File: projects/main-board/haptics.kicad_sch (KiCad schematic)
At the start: 10 parts, among them Q1 ZXTN4240F-7, Q2 ZXTN4240F-7, U12 TLV74330PDBVR

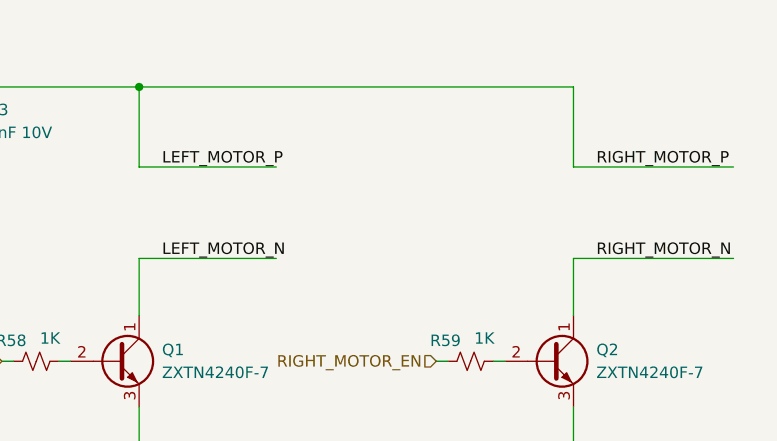
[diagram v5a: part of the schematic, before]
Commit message: Fix footprint DRC errors.
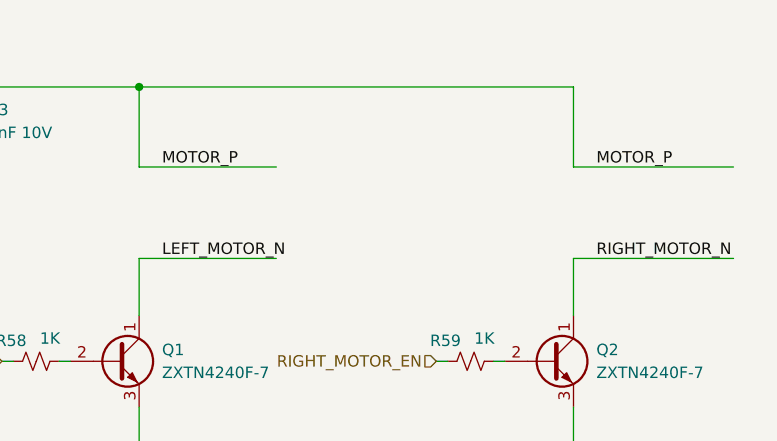
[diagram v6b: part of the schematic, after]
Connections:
- net LEFT_MOTOR_P renamed MOTOR_P
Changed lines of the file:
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@@
 		)
 	)
-	(label "LEFT_MOTOR_P"
+	(label "MOTOR_P"
 		(at 168.91 86.36 0)
 		(effects
@@
 		)
 	)
-	(label "RIGHT_MOTOR_P"
+	(label "MOTOR_P"
 		(at 217.17 86.36 0)
 		(effects

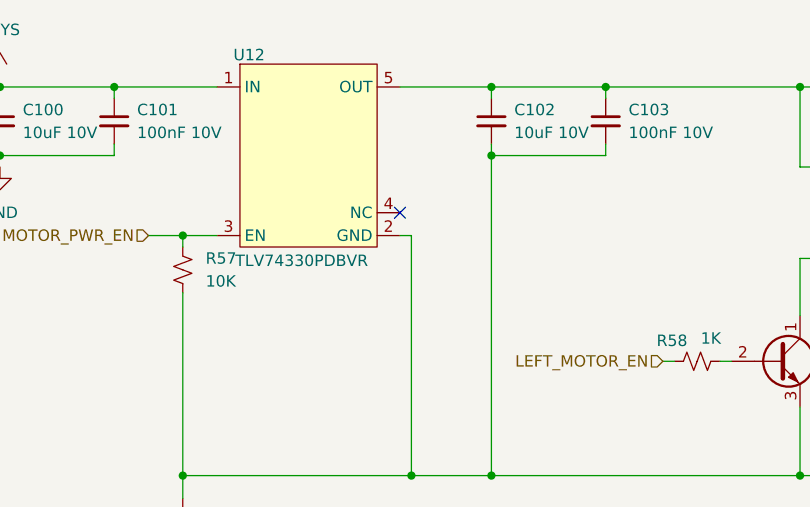
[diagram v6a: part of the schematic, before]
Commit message: Main board PCB layout and routing
- Add 48MHz crystal for STM32
- Add 32kHz crystal for STM32
- Started laying out and routing board
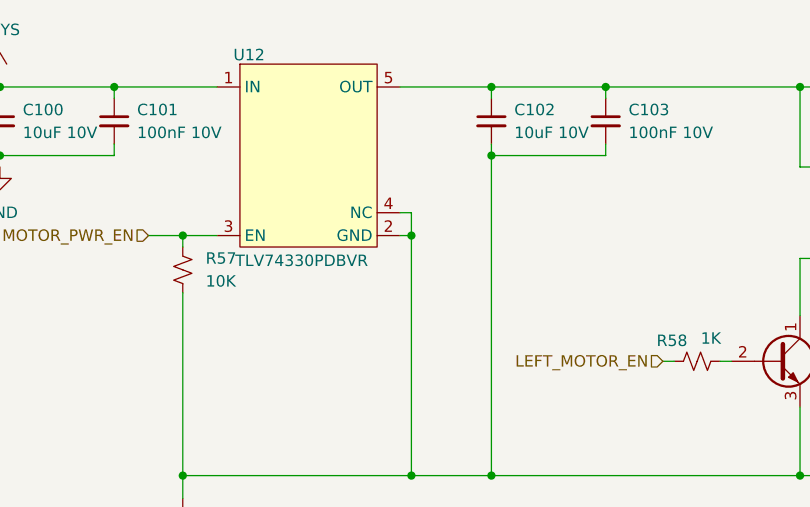
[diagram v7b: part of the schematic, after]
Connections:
- net GND: now also U12.4 (NC)
- no-connect marks 1 -> 0
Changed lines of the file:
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@@
+	)
+	(junction
+		(at 123.19 93.98)
+		(diameter 0)
+		(color 0 0 0 0)
 	)
 	(junction
@@
 		(color 0 0 0 0)
 	)
-	(no_connect
-		(at 121.92 91.44)
+	(wire
+		(pts
+			(xy 132.08 77.47) (xy 132.08 78.74)
+		)
+		(stroke
+			(width 0)
+			(type default)
+		)
 	)
 	(wire
 		(pts
-			(xy 132.08 77.47) (xy 132.08 78.74)
+			(xy 123.19 91.44) (xy 123.19 93.98)
 		)
 		(stroke
@@
 		)
 		(stroke
+			(width 0)
+			(type default)
+		)
+	)
+	(wire
+		(pts
+			(xy 121.92 91.44) (xy 123.19 91.44)
+		)
+		(stroke

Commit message: WIP splitting main board into 3
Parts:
- added NT2: NetTie_2, symbol Device:NetTie_2
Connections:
- net LEFT_MOTOR_N renamed LEFT_MOTOR.N
- net MOTOR_P renamed LEFT_MOTOR.P
- net LEFT_MOTOR.P: now also NT2.1
- net RIGHT_MOTOR_N renamed RIGHT_MOTOR.N
- new net RIGHT_MOTOR.P: NT2.2
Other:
- moved on the sheet: C100, C101
